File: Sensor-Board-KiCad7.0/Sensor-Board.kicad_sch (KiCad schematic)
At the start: 76 parts, among them J2 B04B-XASK-1, U1 OPA396DCKT, U10 BME680, U14 OPA396DCKT, U19 MMBFJ177LT1, U2 OPA396DCKT, U20 MMBFJ177LT1, U21 OPA396DCKT, U22 OPA396DCKT, U25 NAU7802SGI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

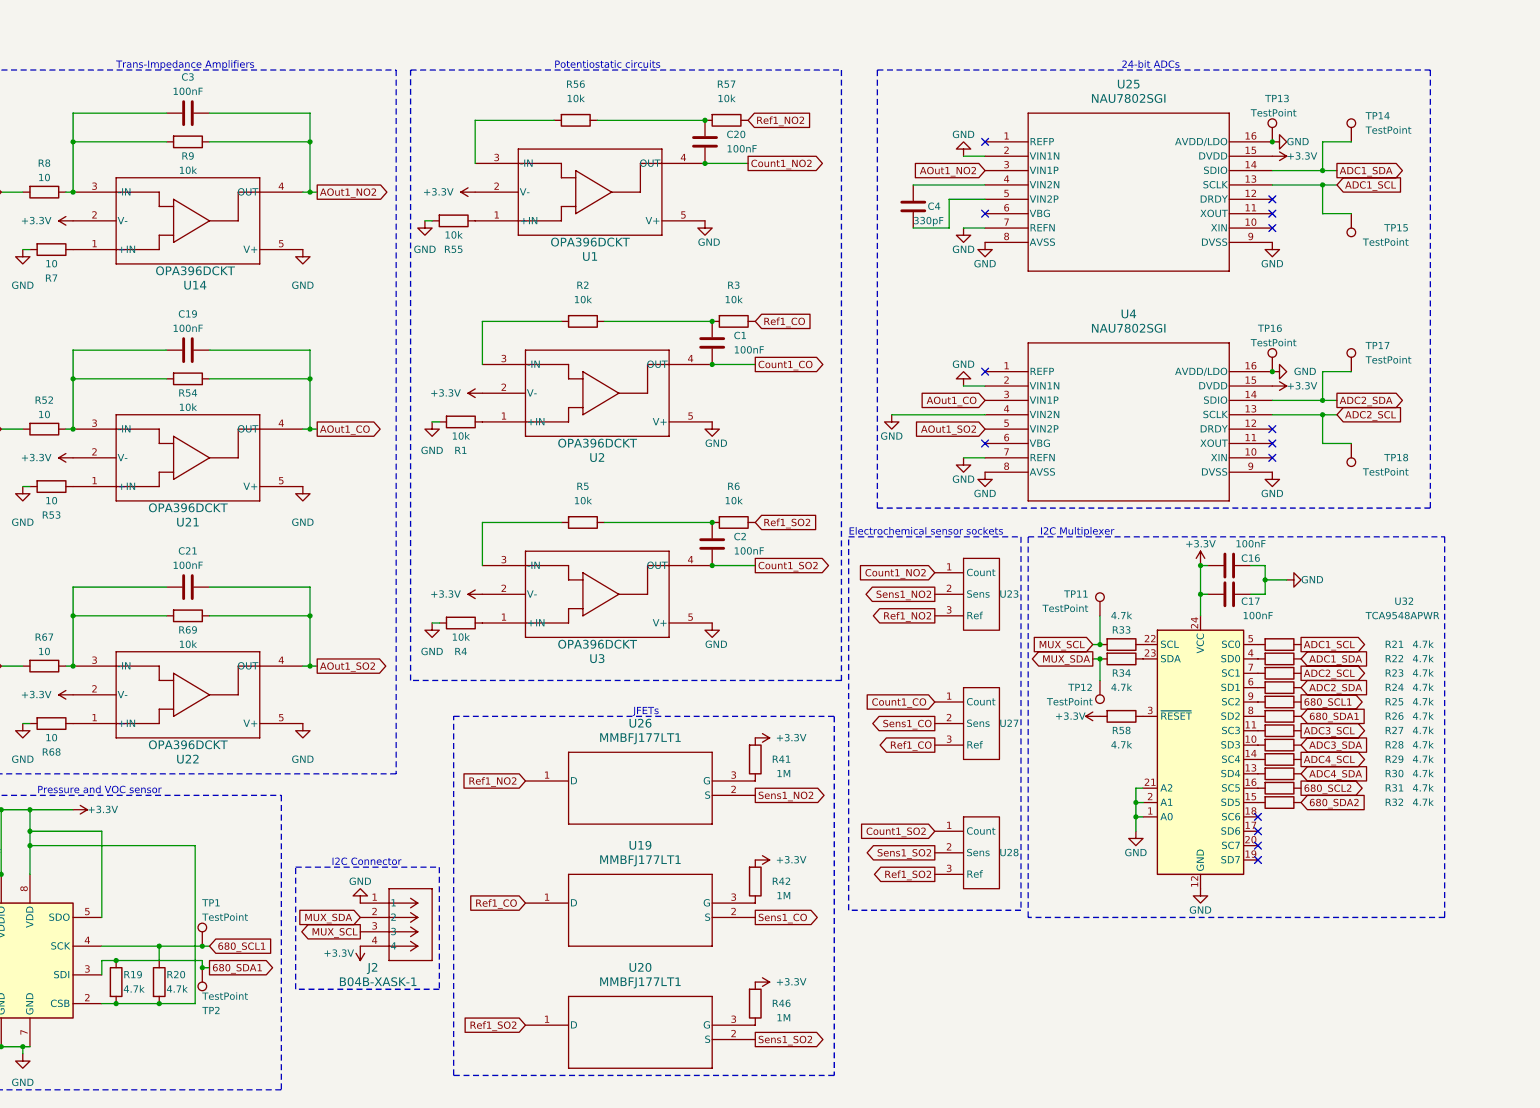
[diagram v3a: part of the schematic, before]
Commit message: Fixed pull-up resistors
Changed all 4.7k to actually be pull-up resistors. Re-organized pcb layout.
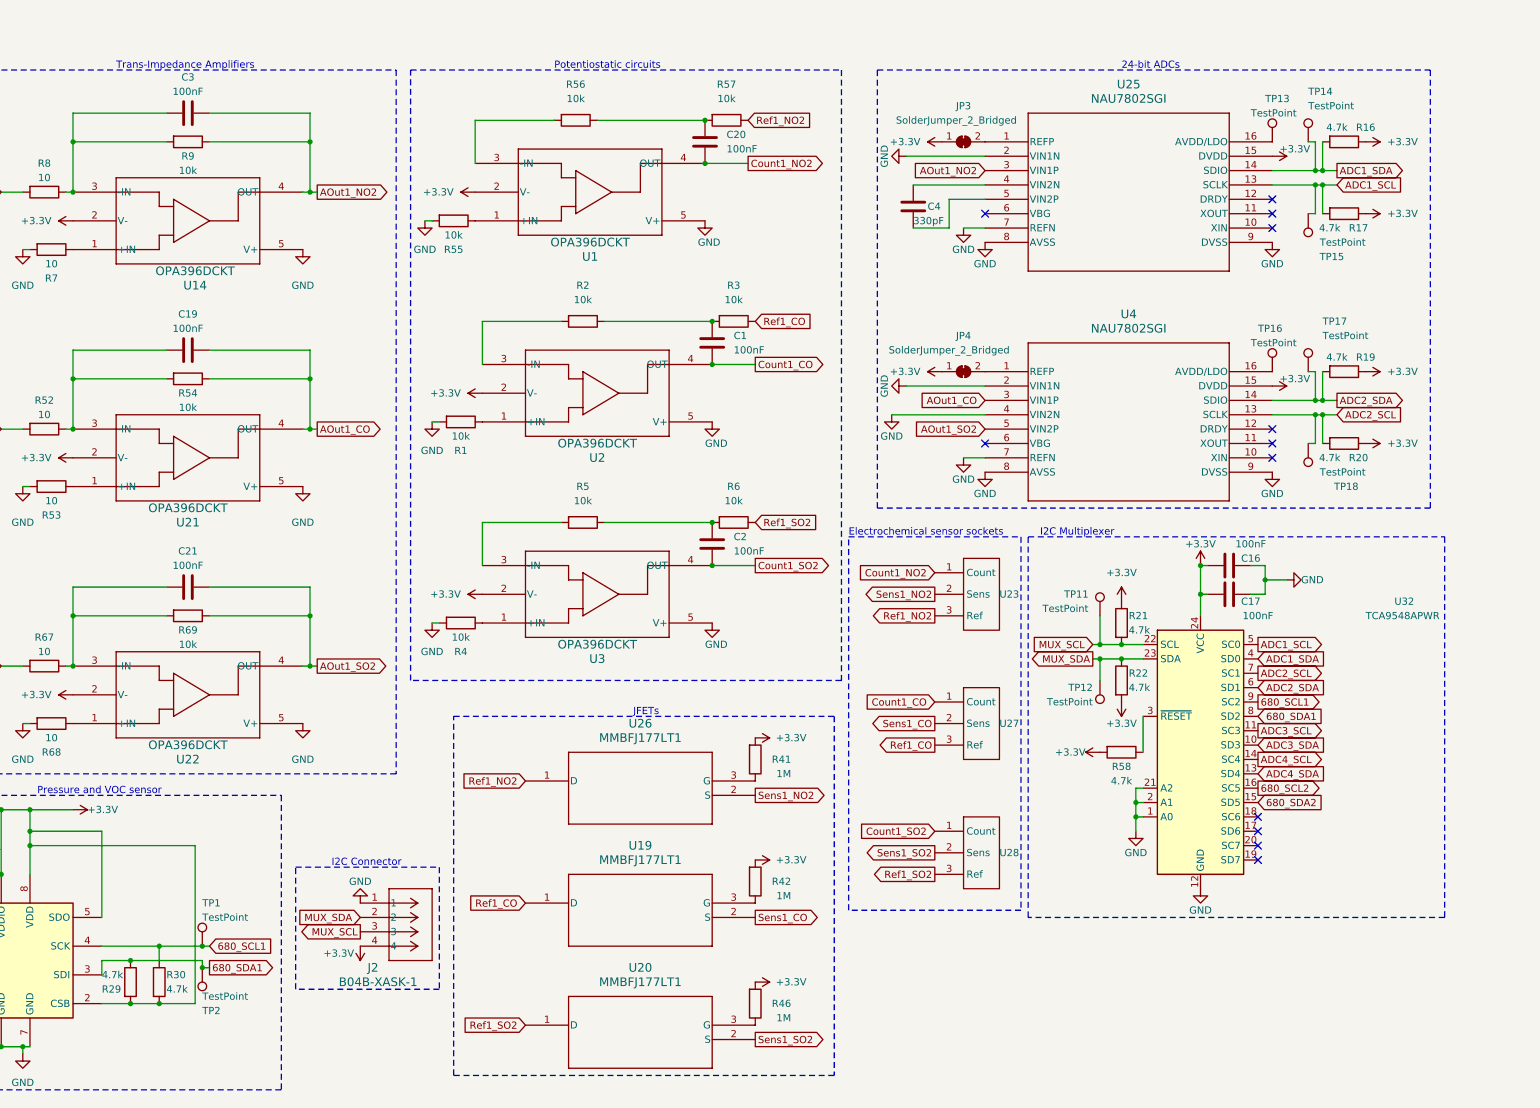
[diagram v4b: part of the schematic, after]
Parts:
- removed R23, R24, R25, R26, R27, R28, R31, R32, R33, R34: 4.7k, Resistor_SMD:R_0603_1608Metric, symbol Device:R
- added JP3, JP4: SolderJumper_2_Bridged, Jumper:SolderJumper-2_P1.3mm_Bridged_RoundedPad1.0x1.5mm, symbol Jumper:SolderJumper_2_Bridged
- added R16, R17: 4.7k, Resistor_SMD:R_0603_1608Metric, symbol Device:R
- R19, R20, R21, R22, R29, R30: LCSC C23162 -> (none)
- R41, R42, R46: LCSC C407640 -> C22935
- U25, U4: Digikey NAU7802SGITR-ND -> NAU7802SGI-ND
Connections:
- net +3.3V: now also R19.1, R20.1, R21.1, R22.2, R29.2, R30.2, JP3.1 (A), JP4.1 (A), R16.1, R17.1; no longer R19.2, R20.2
- net 680_SCL1: now also R30.1, U32.9 (SC2); no longer R20.1
- net 680_SCL2: now also U32.16 (SC5)
- net 680_SDA1: now also R29.1, U32.8 (SD2); no longer R19.1
- net 680_SDA2: now also U32.15 (SD5)
- net ADC1_SCL: now also U32.5 (SC0), R17.2; no longer R21.1
- net ADC1_SDA: now also U32.4 (SD0), R16.2; no longer R22.1
- net ADC2_SCL: now also R20.2, U32.7 (SC1)
- net ADC2_SDA: now also R19.2, U32.6 (SD1)
- net ADC3_SCL: now also U32.11 (SC3)
- net ADC3_SDA: now also U32.10 (SD3)
- net ADC4_SCL: now also U32.14 (SC4); no longer R29.1
- net ADC4_SDA: now also U32.13 (SD4); no longer R30.1
- net GND: no longer TP13.1, TP16.1, U25.16 (AVDD/LDO), U4.16 (AVDD/LDO)
- net MUX_SCL: now also R21.2, U32.22 (SCL)
- net MUX_SDA: now also R22.1, U32.23 (SDA)
- net at U25.1 (REFP): now also JP3.2 (B)
- net at U4.1 (REFP): now also JP4.2 (B)
- new net: TP13.1, U25.16 (AVDD/LDO)
- new net: TP16.1, U4.16 (AVDD/LDO)
- no-connect marks 14 -> 12
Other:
- moved on the sheet: R58, TP14, TP15, TP17, TP18

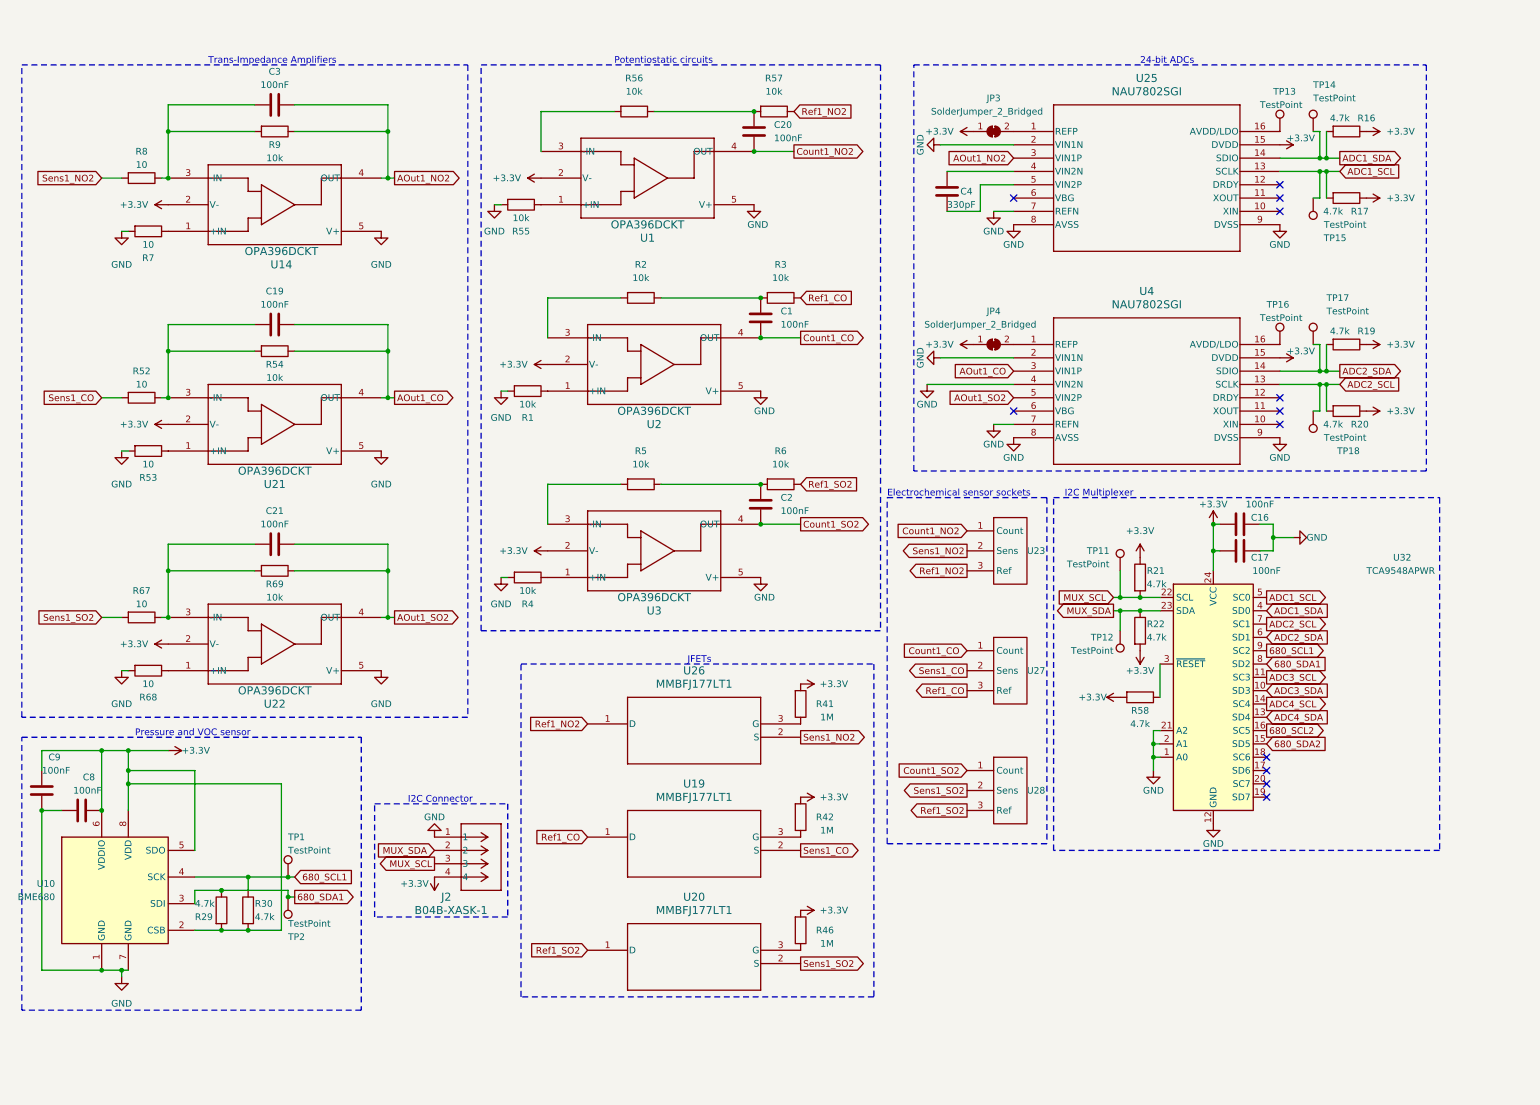
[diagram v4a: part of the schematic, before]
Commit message: Fixed Op-Amp reverse polarity (+misc items)
-Fixed reverse polarity on Op-Amps
-Version bump
-Added power LED
-Moved some components out of keepout zone
-Added emergency 1.65V VRef pad
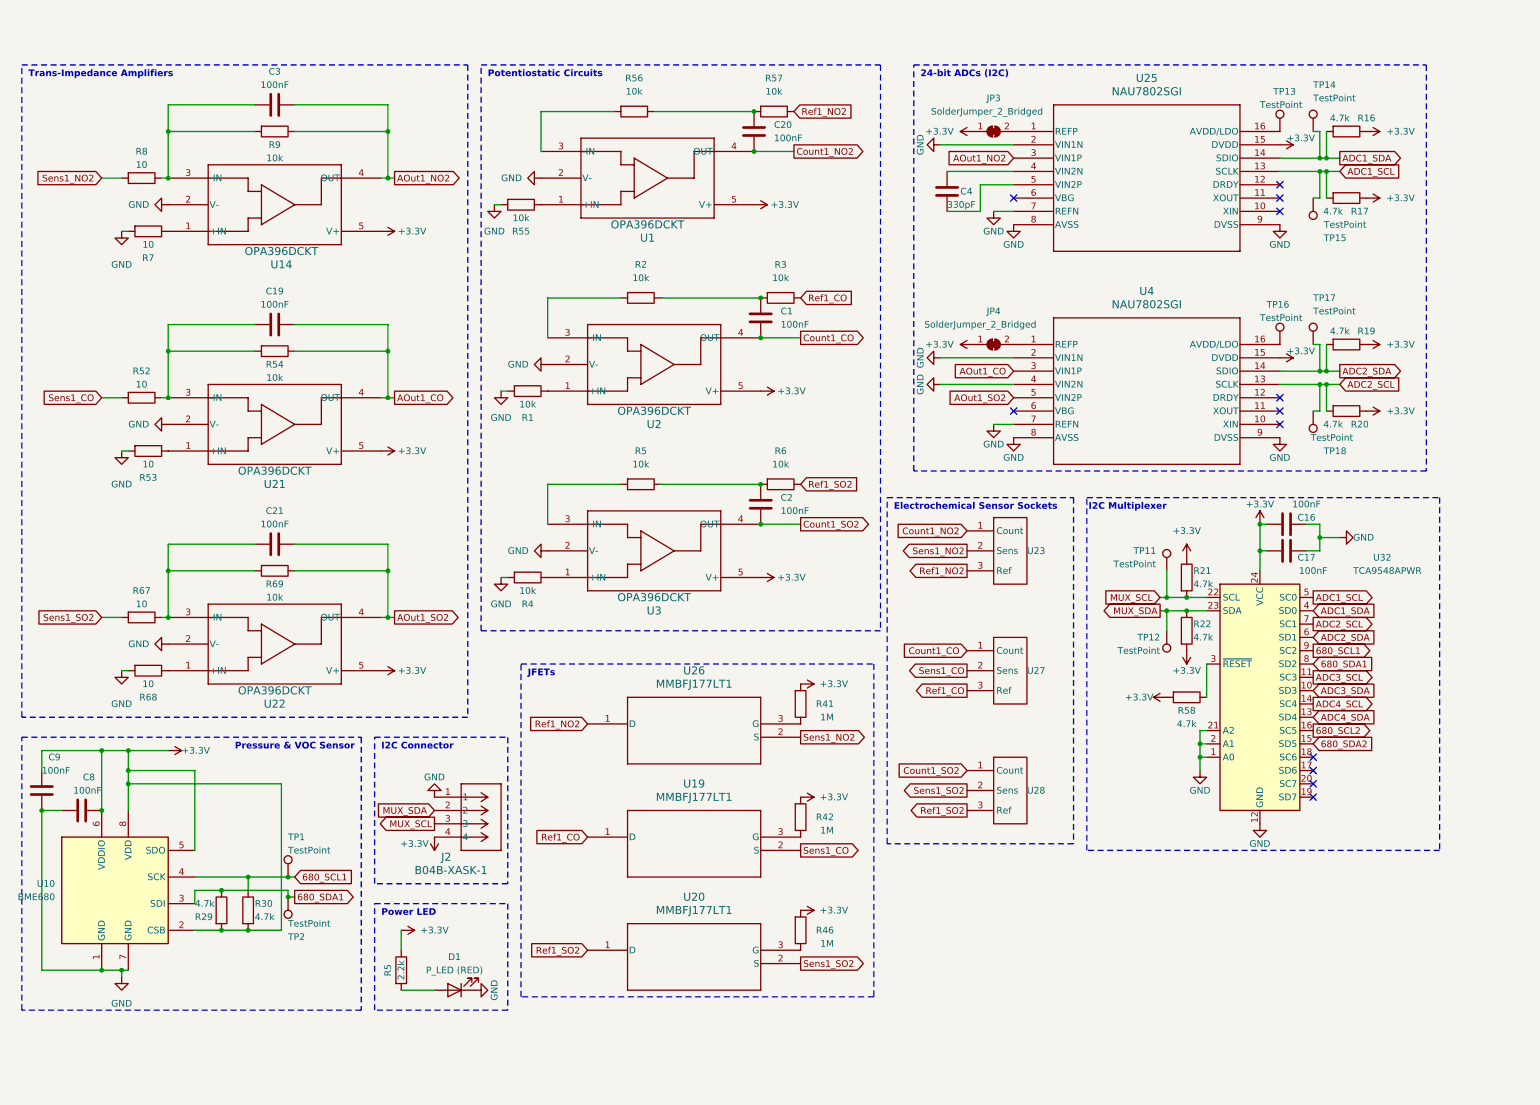
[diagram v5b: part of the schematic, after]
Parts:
- added D1: P_LED (RED), LED_SMD:LED_0603_1608Metric_Pad1.05x0.95mm_HandSolder, symbol Device:LED
- added R5: 2.2k, Resistor_SMD:R_0603_1608Metric_Pad0.98x0.95mm_HandSolder, symbol Device:R
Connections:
- net +3.3V: now also U1.5 (V+), U14.5 (V+), U2.5 (V+), U21.5 (V+), U22.5 (V+), U3.5 (V+), R5.1; no longer U1.2 (V-), U14.2 (V-), U2.2 (V-), U21.2 (V-), U22.2 (V-), U3.2 (V-)
- net GND: now also U1.2 (V-), U14.2 (V-), U2.2 (V-), U21.2 (V-), U22.2 (V-), U3.2 (V-), D1.1 (K); no longer U1.5 (V+), U14.5 (V+), U2.5 (V+), U21.5 (V+), U22.5 (V+), U3.5 (V+)
- new net: D1.2 (A), R5.2
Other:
- note added: "24-bit ADCs (I2C)"
- note added: "Electrochemical Sensor Sockets"
- note added: "Potentiostatic Circuits"
- note added: "Power LED"
- note added: "Pressure & VOC Sensor"
- note removed: "24-bit ADCs"
- note removed: "Electrochemical sensor sockets"
- note removed: "Potentiostatic circuits"
- note removed: "Pressure and VOC sensor"
- moved on the sheet: C16, C17, J2, R21, R22, R58, TP11, TP12, U32
